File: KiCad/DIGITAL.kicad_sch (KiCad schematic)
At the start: 28 parts, among them J7 DE9_Socket, J8 DE9_Pins, SW10 SW_Push, SW11 SW_Push, SW12 SW_Push, SW13 SW_Push, SW14 SW_Push, SW15 SW_Push, SW9 SW_Push, U10 MCP2562-E-SN, U11 MAX3232, U6 24LC256

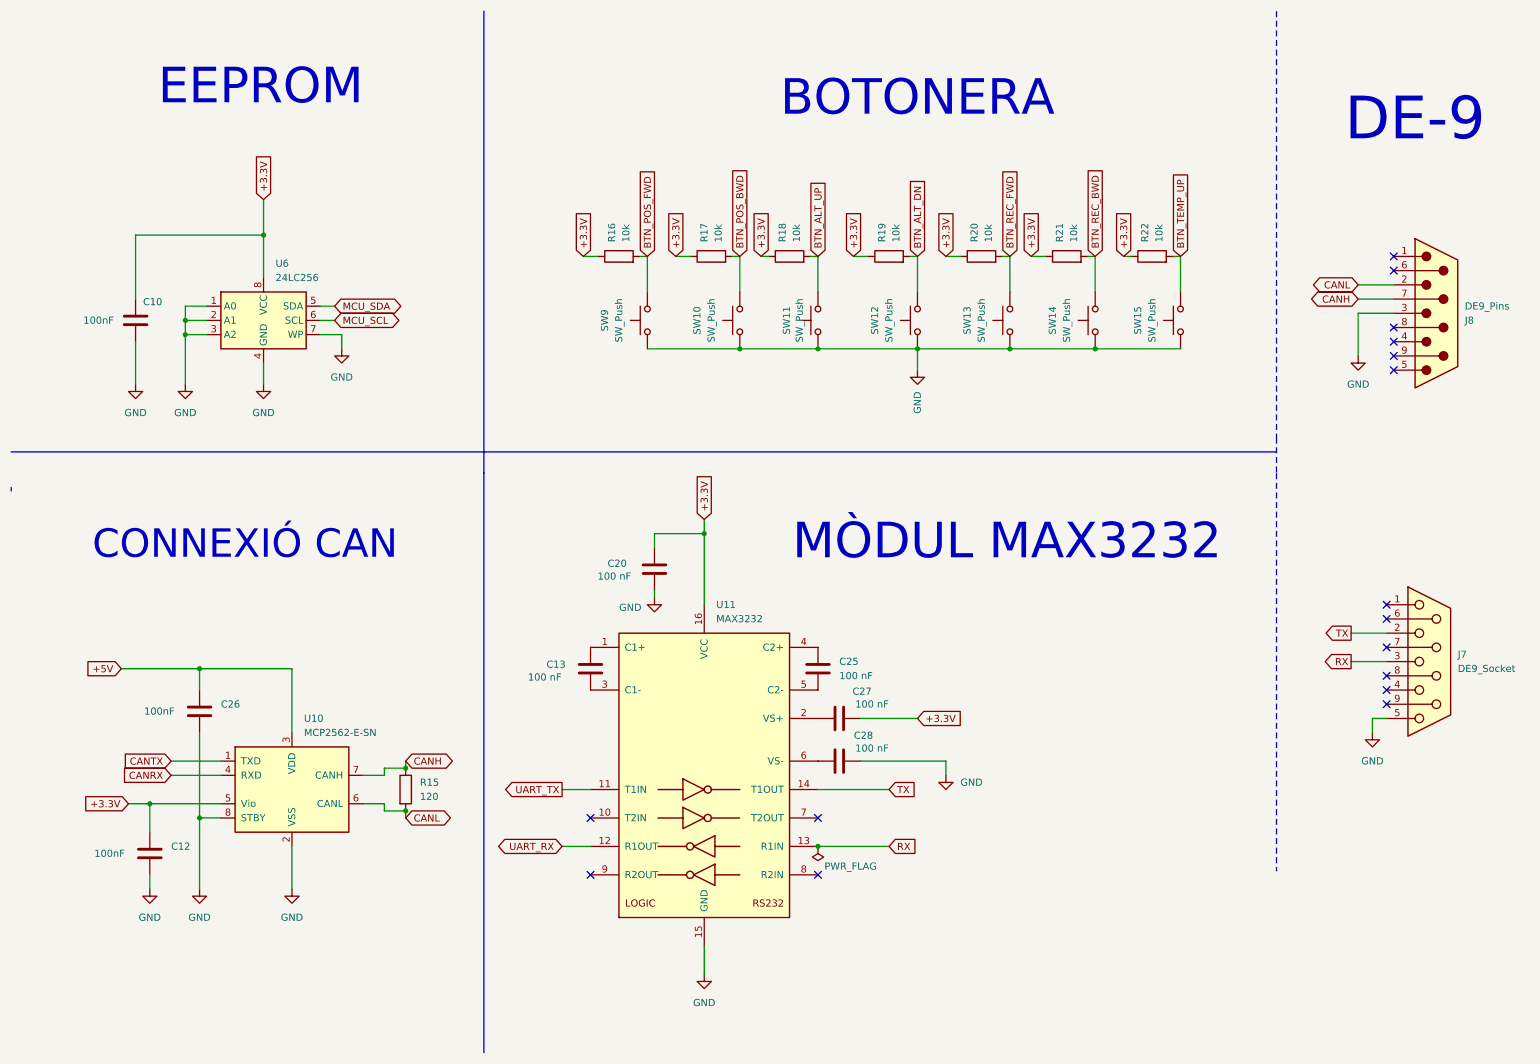
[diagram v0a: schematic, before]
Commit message: Modificació d'errors varis
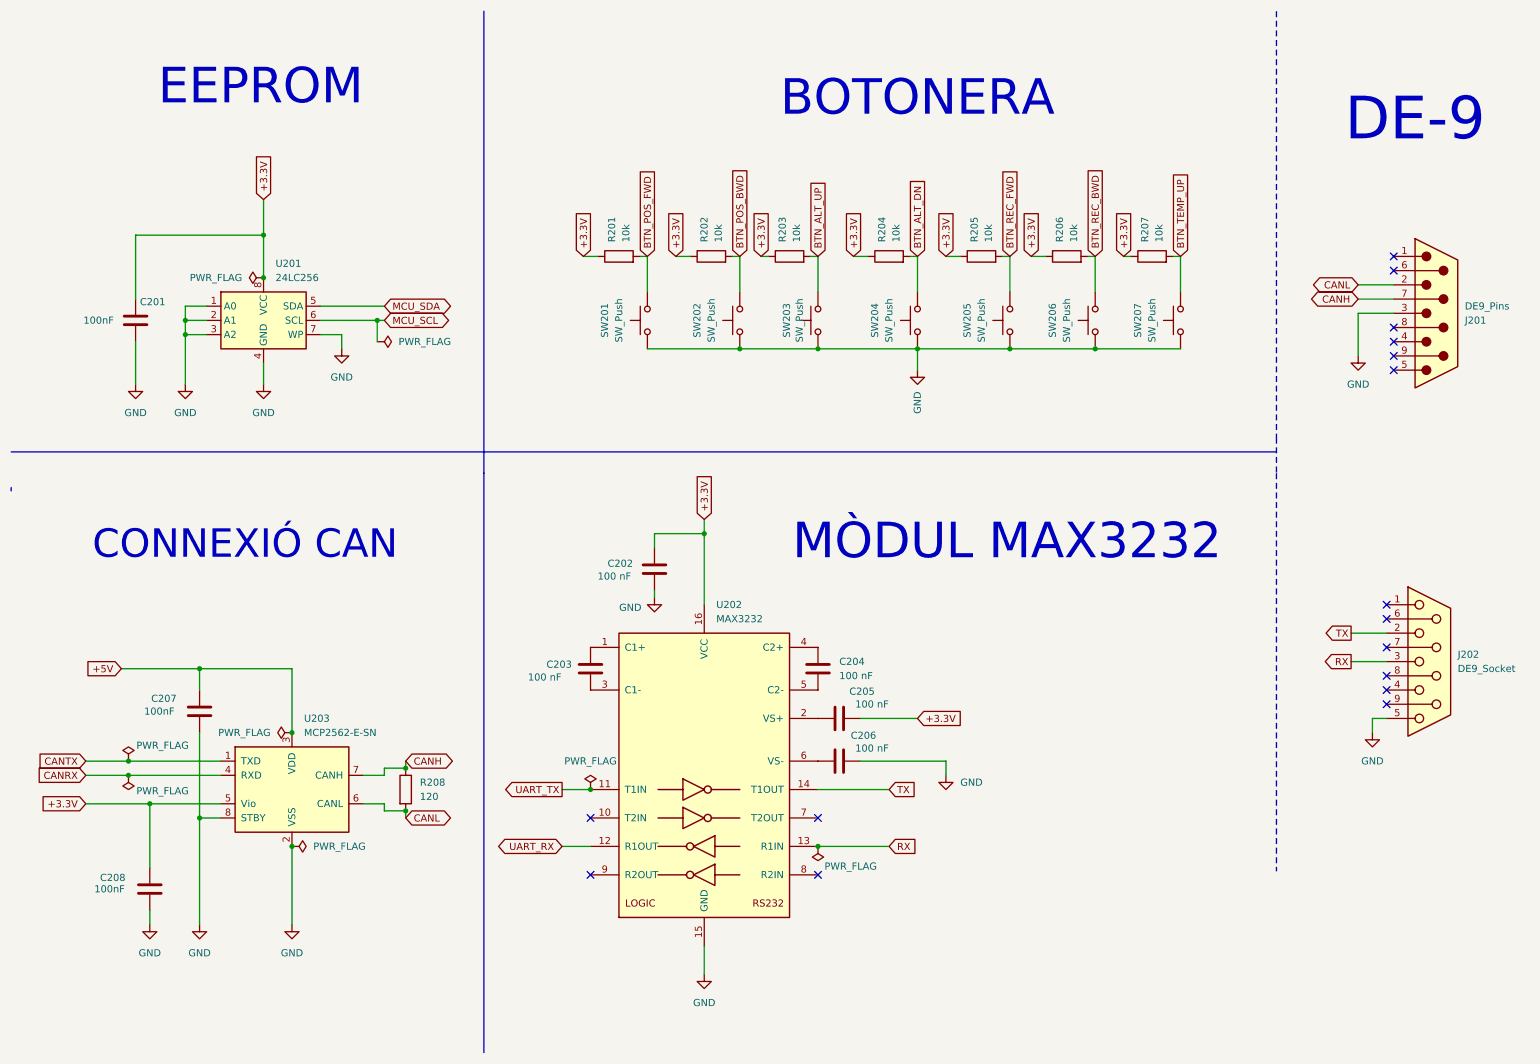
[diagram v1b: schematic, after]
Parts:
- renumbered C10 to C201, C20 to C202, C13 to C203, C25 to C204, C27 to C205, C28 to C206, C26 to C207, C12 to C208, J8 to J201, J7 to J202, R16 to R201, R17 to R202, R18 to R203, R19 to R204, R20 to R205, R21 to R206, R22 to R207, R15 to R208, SW9 to SW201, SW10 to SW202, SW11 to SW203, SW12 to SW204, SW13 to SW205, SW14 to SW206, SW15 to SW207, U6 to U201, U11 to U202, U10 to U203
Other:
- moved on the sheet: C208

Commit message: Modificació d'errors varis
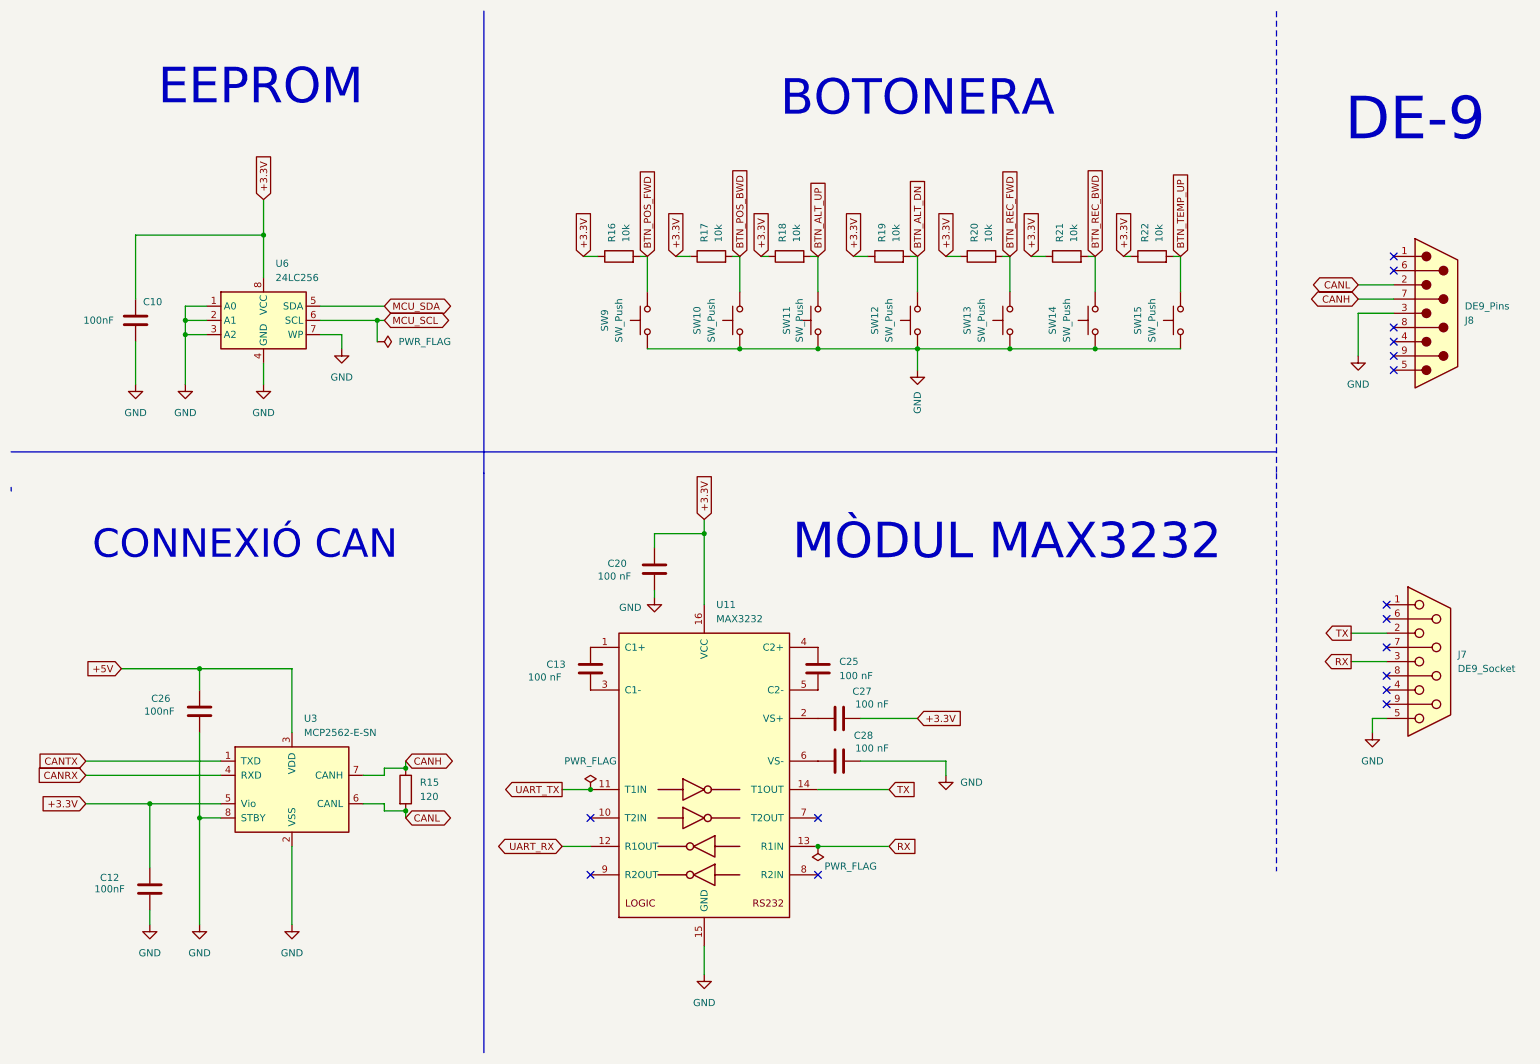
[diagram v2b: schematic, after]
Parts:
- removed U203: MCP2562-E-SN, Package_SO:SOIC-8_3.9x4.9mm_P1.27mm, symbol Interface_CAN_LIN:MCP2562-E-SN
- added U3: MCP2562-E-SN, Package_SO:SOIC-8_3.9x4.9mm_P1.27mm, symbol Interface_CAN_LIN:MCP2562-E-SN
- renumbered C201 to C10, C208 to C12, C203 to C13, C202 to C20, C204 to C25, C207 to C26, C205 to C27, C206 to C28, J202 to J7, J201 to J8, R208 to R15, R201 to R16, R202 to R17, R203 to R18, R204 to R19, R205 to R20, R206 to R21, R207 to R22, SW202 to SW10, SW203 to SW11, SW204 to SW12, SW205 to SW13, SW206 to SW14, SW207 to SW15, SW201 to SW9, U202 to U11, U201 to U6
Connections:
- net +3.3V: now also U3.5 (Vio)
- net +5V: now also U3.3 (VDD)
- net CANH: now also U3.7 (CANH)
- net CANL: now also U3.6 (CANL)
- net CANRX: now also U3.4 (RXD)
- net CANTX: now also U3.1 (TXD)
- net GND: now also U3.2 (VSS), U3.8 (STBY)

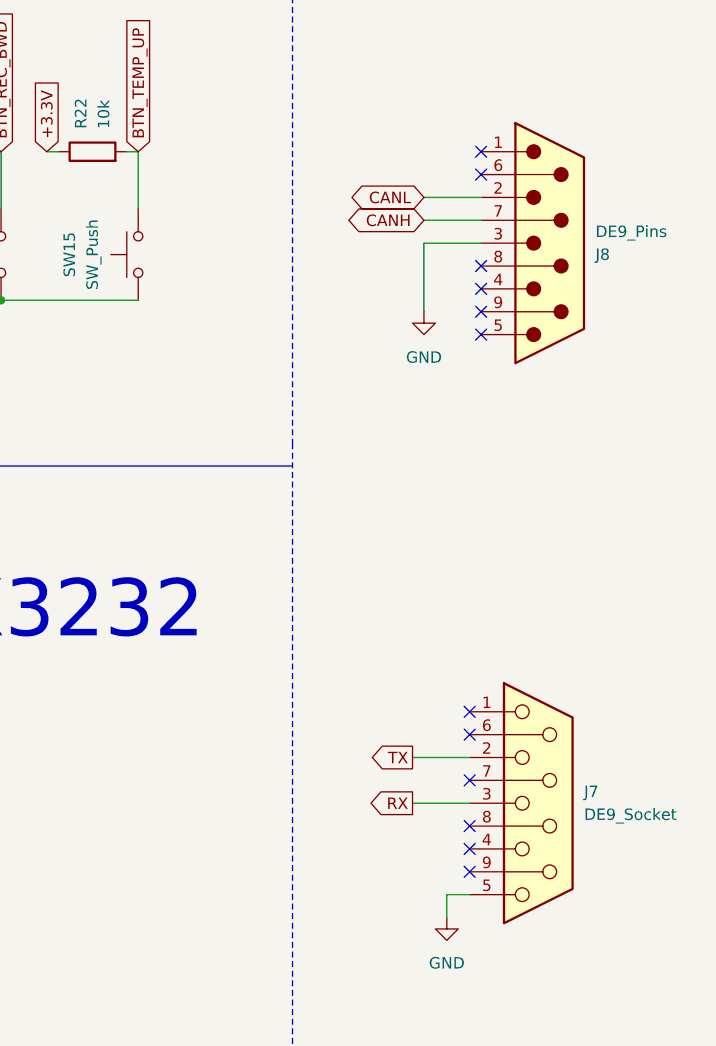
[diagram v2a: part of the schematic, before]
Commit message: Modificació Placement
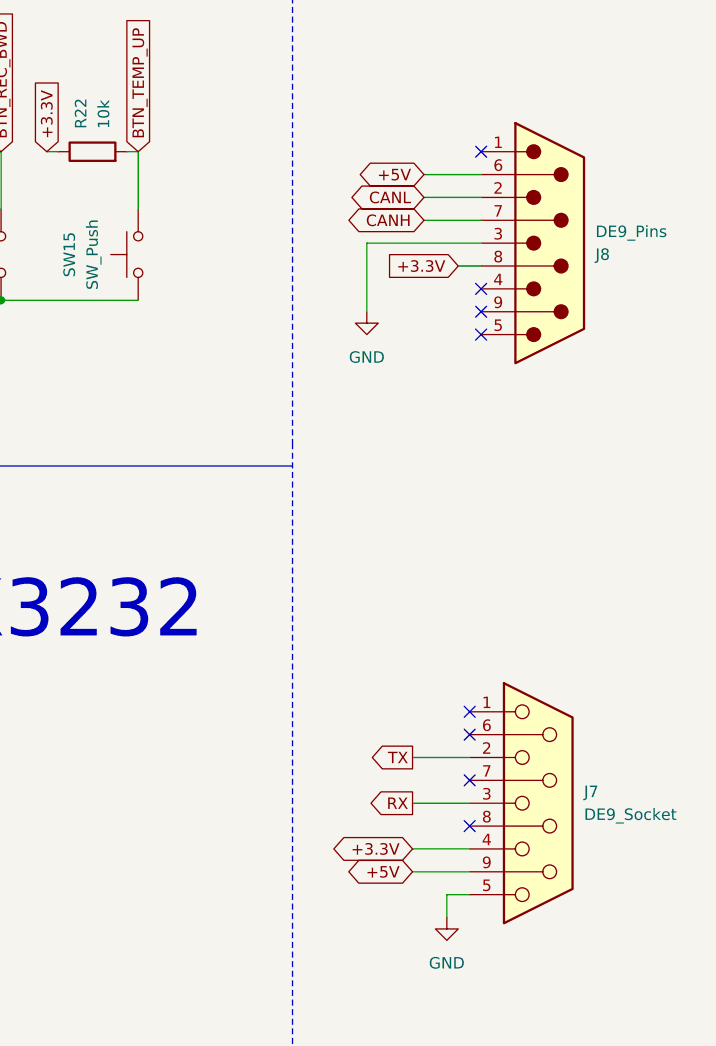
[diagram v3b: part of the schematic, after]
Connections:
- net +3.3V: now also J7.4, J8.8
- net +5V: now also J7.9, J8.6
- no-connect marks 16 -> 12
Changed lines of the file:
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@@
 	)
 	(no_connect
-		(at 257.81 133.35)
-	)
-	(no_connect
-		(at 259.08 58.42)
-	)
-	(no_connect
 		(at 259.08 71.12)
 	)
@@
 	)
 	(no_connect
-		(at 259.08 68.58)
-	)
-	(no_connect
 		(at 259.08 76.2)
 	)
@@
 	)
 	(no_connect
-		(at 257.81 135.89)
-	)
-	(no_connect
 		(at 115.57 166.37)
 	)
@@
 	(wire
 		(pts
+			(xy 252.73 58.42) (xy 259.08 58.42)
+		)
+		(stroke
+			(width 0)
+			(type default)
+		)
+	)
+	(wire
+		(pts
 			(xy 163.83 146.05) (xy 179.07 146.05)
 		)
@@
 	(wire
 		(pts
+			(xy 251.46 133.35) (xy 257.81 133.35)
+		)
+		(stroke
+			(width 0)
+			(type default)
+		)
+	)
+	(wire
+		(pts
 			(xy 36.83 172.72) (xy 36.83 175.26)
 		)
@@
 	(wire
 		(pts
+			(xy 251.46 135.89) (xy 257.81 135.89)
+		)
+		(stroke
+			(width 0)
+			(type default)
+		)
+	)
+	(wire
+		(pts
 			(xy 173.99 62.23) (xy 173.99 55.88)
 		)
@@
 	(wire
 		(pts
-			(xy 252.73 66.04) (xy 252.73 73.66)
+			(xy 246.38 66.04) (xy 246.38 73.66)
 		)
 		(stroke
@@
 	(wire
 		(pts
-			(xy 252.73 66.04) (xy 259.08 66.04)
+			(xy 246.38 66.04) (xy 259.08 66.04)
 		)
 		(stroke
@@
 	(wire
 		(pts
+			(xy 256.54 68.58) (xy 259.08 68.58)
+		)
+		(stroke
+			(width 0)
+			(type default)
+		)
+	)
+	(wire
+		(pts
 			(xy 82.55 146.05) (xy 82.55 147.32)
 		)
@@
 		)
 	)
+	(global_label "+5V"
+		(shape bidirectional)
+		(at 252.73 58.42 180)
+		(fields_autoplaced yes)
+		(effects
+			(font
+				(size 1.27 1.27)
+			)
+			(justify right)
+		)
+		(property "Intersheetrefs" "${INTERSHEET_REFS}"
+			(at 245.576 58.42 0)
+			(effects
+				(font
+					(size 1.27 1.27)
+				)
+				(justify right)
+				(hide yes)
+			)
+		)
+	)
+	(global_label "+5V"
+		(shape bidirectional)
+		(at 251.46 135.89 180)
+		(fields_autoplaced yes)
+		(effects
+			(font
+				(size 1.27 1.27)
+			)
+			(justify right)
+		)
+		(property "Intersheetrefs" "${INTERSHEET_REFS}"
+			(at 244.306 135.89 0)
+			(effects
+				(font
+					(size 1.27 1.27)
+				)
+				(justify right)
+				(hide yes)
+			)
+		)
+	)
 	(global_label "BTN_ALT_DN"
 		(shape input)
@@
 		)
 	)
+	(global_label "+3.3V"
+		(shape input)
+		(at 256.54 68.58 180)
+		(fields_autoplaced yes)
+		(effects
+			(font
+				(size 1.27 1.27)
+			)
+			(justify right)
+		)
+		(property "Intersheetrefs" "${INTERSHEET_REFS}"
+			(at 248.5242 68.58 0)
+			(effects
+				(font
+					(size 1.27 1.27)
+				)
+				(justify right)
+				(hide yes)
+			)
+		)
+	)
 	(global_label "RX"
 		(shape input)
@@
 	)
 	(global_label "+3.3V"
+		(shape bidirectional)
+		(at 251.46 133.35 180)
+		(fields_autoplaced yes)
+		(effects
+			(font
+				(size 1.27 1.27)
+			)
+			(justify right)
+		)
+		(property "Intersheetrefs" "${INTERSHEET_REFS}"
+			(at 242.4917 133.35 0)
+			(effects
+				(font
+					(size 1.27 1.27)
+				)
+				(justify right)
+				(hide yes)
+			)
+		)
+	)
+	(global_label "+3.3V"
 		(shape input)
 		(at 179.07 55.88 90)
@@
 	(symbol
 		(lib_id "power:GND")
-		(at 252.73 73.66 0)
+		(at 246.38 73.66 0)
 		(unit 1)
 		(exclude_from_sim no)
@@
 		(fields_autoplaced yes)
 		(property "Reference" "#PWR031"
-			(at 252.73 80.01 0)
+			(at 246.38 80.01 0)
 			(effects
 				(font
@@
 		)
 		(property "Value" "GND"
-			(at 252.73 78.74 0)
+			(at 246.38 78.74 0)
 			(effects
 				(font
@@
 		)
 		(property "Footprint" ""
-			(at 252.73 73.66 0)
+			(at 246.38 73.66 0)
 			(effects
 				(font
@@
 		)
 		(property "Datasheet" ""
-			(at 252.73 73.66 0)
+			(at 246.38 73.66 0)
 			(effects
 				(font
@@
 		)
 		(property "Description" "Power symbol creates a global label with name \"GND\" , ground"
-			(at 252.73 73.66 0)
+			(at 246.38 73.66 0)
 			(effects
 				(font

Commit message: Routing V1
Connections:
- net +5V: no longer J7.9, J8.6
- no-connect marks 12 -> 14
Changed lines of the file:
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@@
+	)
+	(no_connect
+		(at 257.81 135.89)
 	)
 	(no_connect
@@
 	)
 	(no_connect
+		(at 259.08 58.42)
+	)
+	(no_connect
 		(at 156.21 166.37)
 	)
@@
 	(wire
 		(pts
-			(xy 252.73 58.42) (xy 259.08 58.42)
-		)
-		(stroke
-			(width 0)
-			(type default)
-		)
-	)
-	(wire
-		(pts
 			(xy 163.83 146.05) (xy 179.07 146.05)
 		)
@@
 		(pts
 			(xy 34.29 71.12) (xy 34.29 78.74)
-		)
-		(stroke
-			(width 0)
-			(type default)
-		)
-	)
-	(wire
-		(pts
-			(xy 251.46 135.89) (xy 257.81 135.89)
 		)
 		(stroke
@@
 				(hide yes)
 			)
-		)
-	)
-	(global_label "+5V"
-		(shape bidirectional)
-		(at 252.73 58.42 180)
-		(fields_autoplaced yes)
-		(effects
-			(font
-				(size 1.27 1.27)
-			)
-			(justify right)
-		)
-		(property "Intersheetrefs" "${INTERSHEET_REFS}"
-			(at 245.576 58.42 0)
-			(effects
-				(font
-					(size 1.27 1.27)
-				)
-				(justify right)
-				(hide yes)
-			)
-		)
-	)
-	(global_label "+5V"
-		(shape bidirectional)
-		(at 251.46 135.89 180)
-		(fields_autoplaced yes)
-		(effects
-			(font
-				(size 1.27 1.27)
-			)
-			(justify right)
-		)
-		(property "Intersheetrefs" "${INTERSHEET_REFS}"
-			(at 244.306 135.89 0)
-			(effects
-				(font
-					(size 1.27 1.27)
-				)
-				(justify right)
-				(hide yes)
-			)

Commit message: ROUTING FINAL
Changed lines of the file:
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@@
 	(wire
 		(pts
-			(xy 252.73 63.5) (xy 259.08 63.5)
+			(xy 256.54 63.5) (xy 259.08 63.5)
 		)
 		(stroke
@@
 	(wire
 		(pts
-			(xy 252.73 60.96) (xy 259.08 60.96)
+			(xy 256.54 60.96) (xy 259.08 60.96)
 		)
 		(stroke
@@
 	(global_label "CANL"
 		(shape bidirectional)
-		(at 252.73 60.96 180)
+		(at 256.54 60.96 180)
 		(fields_autoplaced yes)
 		(effects
@@
 		)
 		(property "Intersheetrefs" "${INTERSHEET_REFS}"
-			(at 243.9163 60.96 0)
+			(at 247.7263 60.96 0)
 			(effects
 				(font
@@
 	(global_label "CANH"
 		(shape bidirectional)
-		(at 252.73 63.5 180)
+		(at 256.54 63.5 180)
 		(fields_autoplaced yes)
 		(effects
@@
 		)
 		(property "Intersheetrefs" "${INTERSHEET_REFS}"
-			(at 243.6139 63.5 0)
-			(effects
-				(font
+			(at 247.4239 63.5 0)
+			(effects
+				(font

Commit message: Layout acabado
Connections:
- net GND: now also J8.7; no longer J8.3
- net CANH renamed CAN+
- net CAN+: now also J8.3; no longer J8.7
- net CANL renamed CAN-
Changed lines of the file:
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@@
+	(wire
+		(pts
+			(xy 246.38 63.5) (xy 259.08 63.5)
+		)
+		(stroke
+			(width 0)
+			(type default)
+		)
+	)
 	(wire
 		(pts
@@
 	(wire
 		(pts
-			(xy 256.54 63.5) (xy 259.08 63.5)
+			(xy 256.54 66.04) (xy 259.08 66.04)
 		)
 		(stroke
@@
 	(wire
 		(pts
+			(xy 246.38 63.5) (xy 246.38 73.66)
+		)
+		(stroke
+			(width 0)
+			(type default)
+		)
+	)
+	(wire
+		(pts
 			(xy 36.83 153.67) (xy 36.83 165.1)
 		)
@@
 	(wire
 		(pts
+			(xy 205.74 72.39) (xy 220.98 72.39)
+		)
+		(stroke
+			(width 0)
+			(type default)
+		)
+	)
+	(wire
+		(pts
 			(xy 256.54 60.96) (xy 259.08 60.96)
 		)
@@
 	(wire
 		(pts
-			(xy 205.74 72.39) (xy 220.98 72.39)
-		)
-		(stroke
-			(width 0)
-			(type default)
-		)
-	)
-	(wire
-		(pts
 			(xy 194.31 55.88) (xy 196.85 55.88)
 		)
@@
 	(wire
 		(pts
-			(xy 246.38 66.04) (xy 246.38 73.66)
-		)
-		(stroke
-			(width 0)
-			(type default)
-		)
-	)
-	(wire
-		(pts
 			(xy 57.15 52.07) (xy 57.15 59.69)
-		)
-		(stroke
-			(width 0)
-			(type default)
-		)
-	)
-	(wire
-		(pts
-			(xy 246.38 66.04) (xy 259.08 66.04)
 		)
 		(stroke
@@
 		)
 	)
-	(global_label "CANL"
+	(global_label "CAN-"
 		(shape bidirectional)
 		(at 256.54 60.96 180)
@@
 		)
 		(property "Intersheetrefs" "${INTERSHEET_REFS}"
-			(at 247.7263 60.96 0)
+			(at 247.995 60.96 0)
 			(effects
 				(font
@@
 		)
 	)
-	(global_label "CANL"
+	(global_label "CAN-"
 		(shape bidirectional)
 		(at 82.55 156.21 0)
@@
 		)
 		(property "Intersheetrefs" "${INTERSHEET_REFS}"
-			(at 91.3637 156.21 0)
+			(at 91.095 156.21 0)
 			(effects
 				(font
@@
 		)
 	)
-	(global_label "CANH"
+	(global_label "CAN+"
 		(shape bidirectional)
 		(at 82.55 146.05 0)
@@
 		)
 		(property "Intersheetrefs" "${INTERSHEET_REFS}"
-			(at 91.6661 146.05 0)
+			(at 91.095 146.05 0)
 			(effects
 				(font
@@
 		)
 	)
-	(global_label "CANH"
+	(global_label "CAN+"
 		(shape bidirectional)
-		(at 256.54 63.5 180)
+		(at 256.54 66.04 180)
 		(fields_autoplaced yes)
 		(effects
@@
 		)
 		(property "Intersheetrefs" "${INTERSHEET_REFS}"
-			(at 247.4239 63.5 0)
-			(effects
-				(font
+			(at 247.995 66.04 0)
+			(effects
+				(font
